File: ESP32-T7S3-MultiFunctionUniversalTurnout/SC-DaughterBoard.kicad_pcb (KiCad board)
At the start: 2 copper layers, 33 x 72.4 mm, 1 part, among them J101 IO_Port

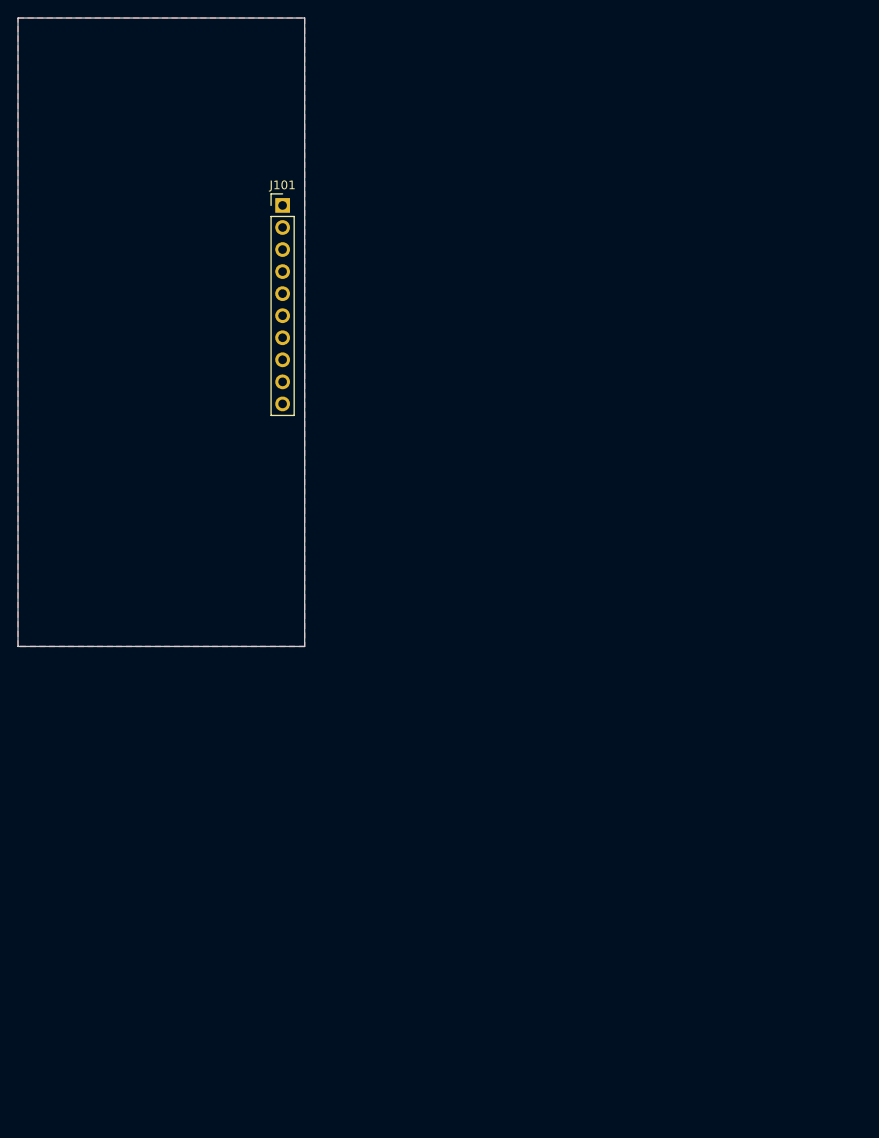
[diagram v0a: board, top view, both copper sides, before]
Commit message: Completed single coil Turnout Daughter board.
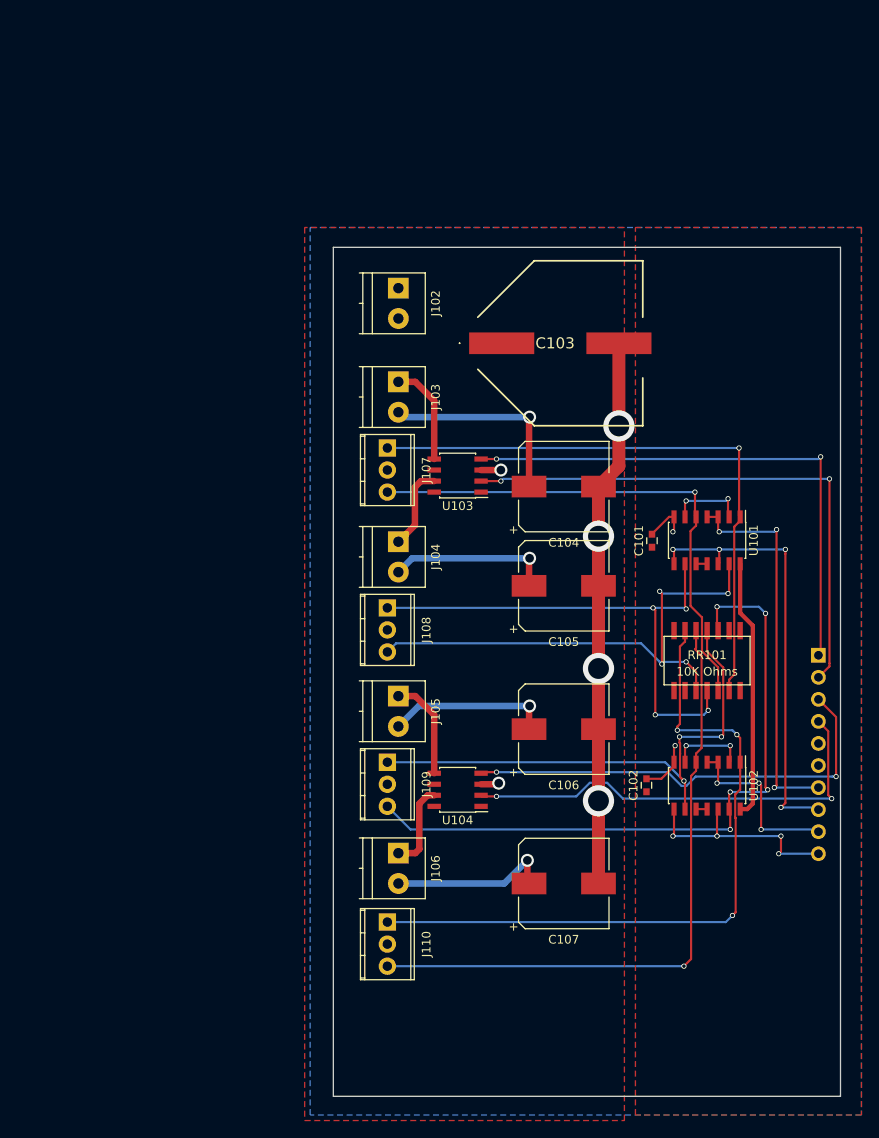
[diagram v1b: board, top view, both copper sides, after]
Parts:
- added C101: .1 uf, Capacitors_SMD:C_0603, F.Cu at (98.4, 85.6)
- added C102: .1 uf, Capacitors_SMD:C_0603, F.Cu at (97.8, 113.8)
- added C103: 4700uf 25V, BigSMDCaps:EEEFK0J133SM, F.Cu at (87.9, 62.9)
- added C104: 1000uf 25V, Capacitors_SMD:CP_Elec_10x10.5, F.Cu at (88.3, 79.4)
- added C105: 1000uf 25V, Capacitors_SMD:CP_Elec_10x10.5, F.Cu at (88.3, 90.8)
- added C106: 1000uf 25V, Capacitors_SMD:CP_Elec_10x10.5, F.Cu at (88.3, 107.3)
- added C107: 1000uf 25V, Capacitors_SMD:CP_Elec_10x10.5, F.Cu at (88.3, 125.1)
- added J102: - 12-15 +, Connectors_Terminal_Blocks:TerminalBlock_Pheonix_PT-3.5mm_2pol, F.Cu at (69.2, 56.5)
- added J103: Motor 1, Terminal_Blocks:TerminalBlock_Pheonix_PT-3.5mm_2pol, F.Cu at (69.2, 67.3)
- added J104: Motor 2, Terminal_Blocks:TerminalBlock_Pheonix_PT-3.5mm_2pol, F.Cu at (69.2, 85.7)
- added J105: Motor 3, Terminal_Blocks:TerminalBlock_Pheonix_PT-3.5mm_2pol, F.Cu at (69.2, 103.5)
- added J106: Motor 4, Terminal_Blocks:TerminalBlock_Pheonix_PT-3.5mm_2pol, F.Cu at (69.2, 121.6)
- added J107: P1A G P1B, Connectors_Terminal_Blocks:TerminalBlock_Pheonix_MPT-2.54mm_3pol, F.Cu at (67.9, 74.9)
- added J108: P2A G P2B, Connectors_Terminal_Blocks:TerminalBlock_Pheonix_MPT-2.54mm_3pol, F.Cu at (67.9, 93.3)
- added J109: P4A G P4B, Connectors_Terminal_Blocks:TerminalBlock_Pheonix_MPT-2.54mm_3pol, F.Cu at (67.9, 111.1)
- added J110: P3A G P3B, Connectors_Terminal_Blocks:TerminalBlock_Pheonix_MPT-2.54mm_3pol, F.Cu at (67.9, 129.5)
- added RR101: 10K Ohms, 48xxP:4814P, F.Cu at (104.8, 99.4)
- added U101: 74HCT00, Housings_SOIC:SOIC-14_3.9x8.7mm_Pitch1.27mm, F.Cu at (104.8, 85.6)
- added U102: 74HCT00, Housings_SOIC:SOIC-14_3.9x8.7mm_Pitch1.27mm, F.Cu at (104.8, 113.8)
- added U103: TC4427, Housings_SOIC:SOIC-8_3.9x4.9mm_Pitch1.27mm, F.Cu at (76.0, 78.1)
- added U104: TC4427, Housings_SOIC:SOIC-8_3.9x4.9mm_Pitch1.27mm, F.Cu at (76.0, 114.3)
- J101: moved to B.Cu
- moved J101 80.6 mm to (117.6, 98.8), turned to 180 degrees
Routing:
- net /P3A: track 0.00 -> 80.4 mm, vias 0 -> 3
- net GND: track 0.00 -> 78.9 mm, vias 0 -> 8
- net /P4B: track 0.00 -> 78.6 mm, vias 0 -> 5
- net /P3B: track 0.00 -> 74.0 mm, vias 0 -> 1
- net /P1A: track 0.00 -> 69.0 mm, vias 0 -> 1
- net /Motor2: track 0.00 -> 63.6 mm, vias 0 -> 2
- net /Motor1: track 0.00 -> 62.2 mm, vias 0 -> 2
- net /P4A: track 0.00 -> 61.6 mm, vias 0 -> 3
- net /P2A: track 0.00 -> 60.8 mm, vias 0 -> 4
- net /P1B: track 0.00 -> 59.9 mm, vias 0 -> 1
- net /P2B: track 0.00 -> 59.7 mm, vias 0 -> 4
- net /Motor3: track 0.00 -> 51.8 mm, vias 0 -> 2
- net /Motor4: track 0.00 -> 51.4 mm, vias 0 -> 2
- net /Points2: track 0.00 -> 50.7 mm, vias 0 -> 4
- net /Points1: track 0.00 -> 44.7 mm, vias 0 -> 3
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- added copper zone on F.Cu, net MotorPower
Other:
- board size 33 x 72.4 mm -> 58.4 x 97.8 mm

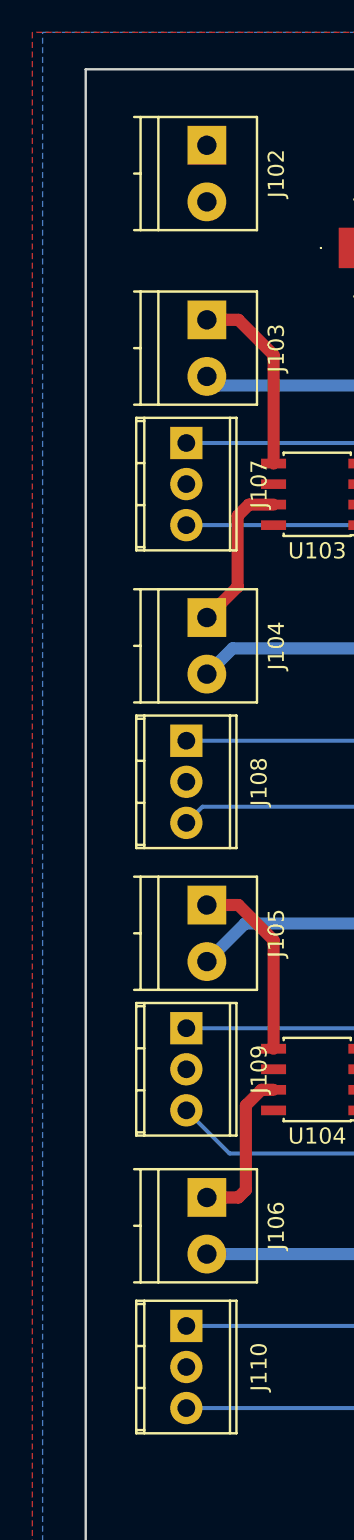
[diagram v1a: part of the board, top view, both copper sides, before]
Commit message: Completed turnout daughterboards.
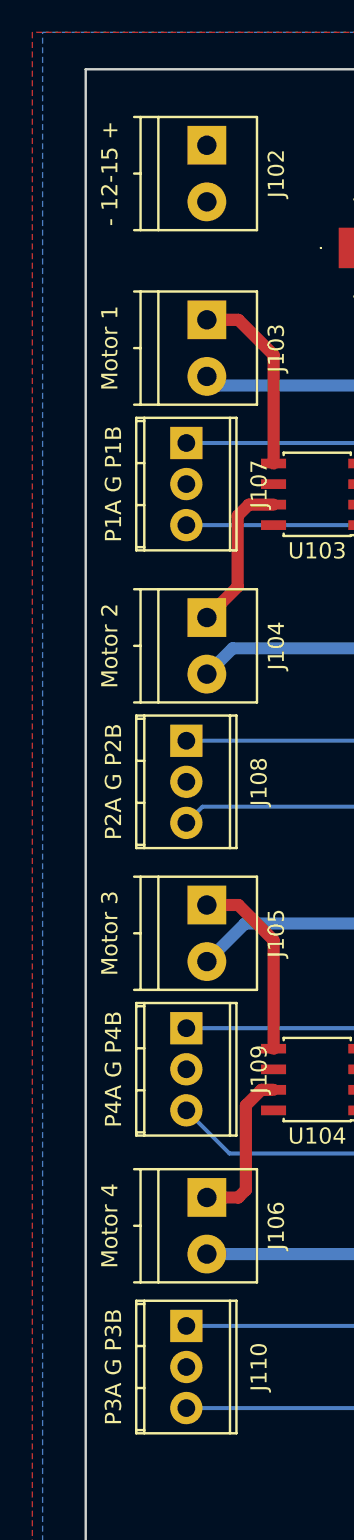
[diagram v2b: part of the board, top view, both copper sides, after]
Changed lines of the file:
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@@
     (links 64)
     (no_connects 0)
-    (area 61.646999 51.740999 120.217001 149.681001)
+    (area 58.42 49.53 139.422 152.400001)
     (thickness 1.6)
     (drawings 8)
@@
       (effects (font (size 1 1) (thickness 0.15)))
     )
-    (fp_text value "- 12-15 +" (at 1.75 6 270) (layer F.Fab)
+    (fp_text value "- 12-15 +" (at 1.75 6 270) (layer F.SilkS)
       (effects (font (size 1 1) (thickness 0.15)))
     )
@@
       (effects (font (size 1 1) (thickness 0.15)))
     )
-    (fp_text value "Motor 1" (at 1.75 6 270) (layer F.Fab)
+    (fp_text value "Motor 1" (at 1.75 6 270) (layer F.SilkS)
       (effects (font (size 1 1) (thickness 0.15)))
     )
@@
       (effects (font (size 1 1) (thickness 0.15)))
     )
-    (fp_text value "Motor 2" (at 1.75 6 270) (layer F.Fab)
+    (fp_text value "Motor 2" (at 1.75 6 270) (layer F.SilkS)
       (effects (font (size 1 1) (thickness 0.15)))
     )
@@
       (effects (font (size 1 1) (thickness 0.15)))
     )
-    (fp_text value "Motor 3" (at 1.75 6 270) (layer F.Fab)
+    (fp_text value "Motor 3" (at 1.75 6 270) (layer F.SilkS)
       (effects (font (size 1 1) (thickness 0.15)))
     )
@@
       (effects (font (size 1 1) (thickness 0.15)))
     )
-    (fp_text value "Motor 4" (at 1.75 6 270) (layer F.Fab)
+    (fp_text value "Motor 4" (at 1.75 6 270) (layer F.SilkS)
       (effects (font (size 1 1) (thickness 0.15)))
     )
@@
       (effects (font (size 1 1) (thickness 0.15)))
     )
-    (fp_text value "P1A G P1B" (at 2.54 4.50088 270) (layer F.Fab)
+    (fp_text value "P1A G P1B" (at 2.54 4.50088 270) (layer F.SilkS)
       (effects (font (size 1 1) (thickness 0.15)))
     )
@@
       (effects (font (size 1 1) (thickness 0.15)))
     )
-    (fp_text value "P2A G P2B" (at 2.54 4.50088 270) (layer F.Fab)
+    (fp_text value "P2A G P2B" (at 2.54 4.50088 270) (layer F.SilkS)
       (effects (font (size 1 1) (thickness 0.15)))
     )
@@
       (effects (font (size 1 1) (thickness 0.15)))
     )
-    (fp_text value "P4A G P4B" (at 2.54 4.50088 270) (layer F.Fab)
+    (fp_text value "P4A G P4B" (at 2.54 4.50088 270) (layer F.SilkS)
       (effects (font (size 1 1) (thickness 0.15)))
     )
@@
       (effects (font (size 1 1) (thickness 0.15)))
     )
-    (fp_text value "P3A G P3B" (at 2.54 4.50088 270) (layer F.Fab)
-      (effects (font (size 1 1) (thickness 0.15)))
-    )
+    (fp_text value "P3A G P3B" (at 2.54 4.50088 270) (layer F.SilkS)
+      (effects (font (size 1 1) (thickness 0.15)))
+    )

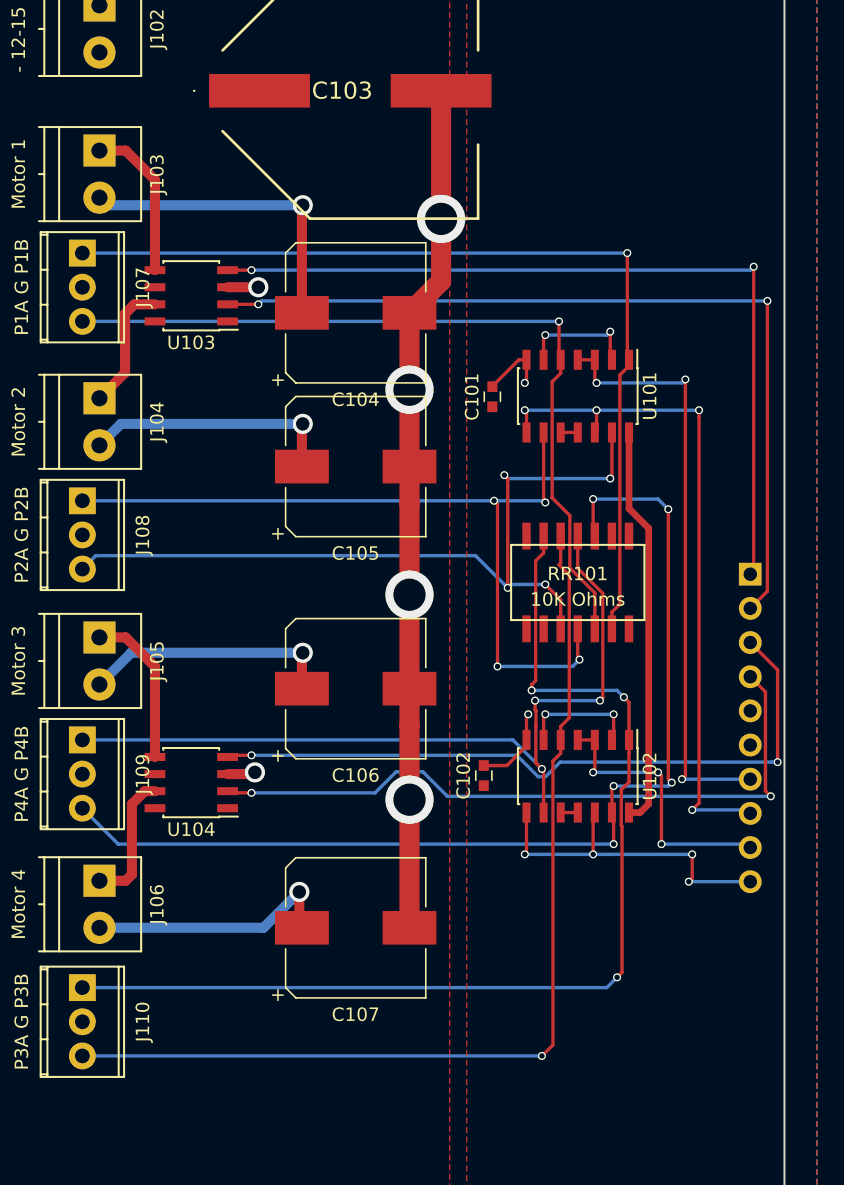
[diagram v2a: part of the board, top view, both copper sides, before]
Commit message: Add support standoffs for turnout daughter boards.
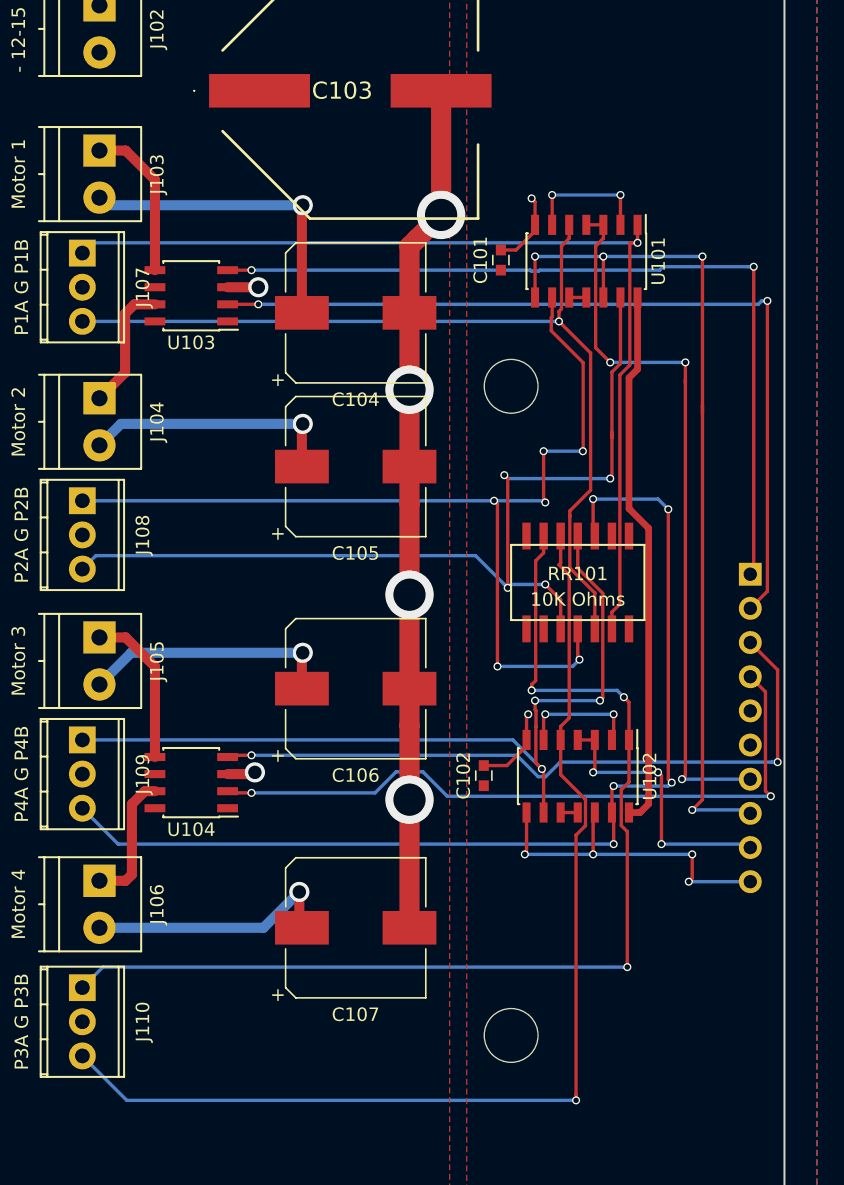
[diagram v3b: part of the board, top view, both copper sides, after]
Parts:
- added REF**: MountingHole_4mm, Mounting_Holes:MountingHole_4mm, F.Cu at (99.8, 84.8)
- added REF**: MountingHole_4mm, Mounting_Holes:MountingHole_4mm, F.Cu at (99.8, 133.1)
- moved C101 10.2 mm to (99.1, 75.5)
- moved U101 10.1 mm to (105.4, 75.5)
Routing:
- net /Points2: track 50.7 -> 65.0 mm
- net /P2A: track 60.8 -> 74.8 mm, vias 4 -> 6
- net /P2B: track 59.7 -> 70.3 mm
- net +3V3: track 29.9 -> 40.2 mm
- net /Points1: track 44.7 -> 54.2 mm
- net /P1B: track 59.9 -> 68.2 mm
- net /P3B: track 74.0 -> 81.7 mm
- net /P1A: track 69.0 -> 72.7 mm
- net Net-(U101-Pad2): track 8.97 -> 9.52 mm

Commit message: Final checks.
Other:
- board text added: "1"
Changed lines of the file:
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@@
     (links 64)
     (no_connects 0)
-    (area 58.42 49.53 149.963 159.672001)
+    (area 61.646999 51.740999 120.217001 149.681001)
     (thickness 1.6)
-    (drawings 11)
+    (drawings 13)
     (tracks 341)
     (zones 0)
@@
     (38 B.Mask user)
     (39 F.Mask user)
-    (40 Dwgs.User user hide)
+    (40 Dwgs.User user)
     (41 Cmts.User user)
     (42 Eco1.User user)
@@
     (visible_elements FFFFFF7F)
     (pcbplotparams
-      (layerselection 0x00030_80000001)
-      (usegerberextensions false)
+      (layerselection 0x3ffff_80000001)
+      (usegerberextensions true)
       (excludeedgelayer true)
       (linewidth 0.100000)
@@
       (outputformat 1)
       (mirror false)
-      (drillshape 1)
+      (drillshape 0)
       (scaleselection 1)
-      (outputdirectory ""))
+      (outputdirectory Gerber/))
   )
   (net 0 "")
@@
     )
   )
+  (gr_text 1 (at 99.441 102.87) (layer F.Fab)
+    (effects (font (size 1 1) (thickness 0.15)))
+  )
+  (gr_circle (center 100.838 100.711) (end 101.473 101.092) (layer F.SilkS) (width 0.2))
   (dimension 48.641 (width 0.3) (layer Dwgs.User)
     (gr_text "48.641 mm" (at 143.463 108.6485 90) (layer Dwgs.User)
